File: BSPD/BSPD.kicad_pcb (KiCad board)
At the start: 2 copper layers, 66 x 42 mm, 66 parts, among them J2 282834-6, K2 G5Q-1A, Q1 BSS84, Q2 MMBT2222A, Q3 MMBT2222A, U1 LM339, U2 LM339, U3 74LVC2G00, U5 74LVC2G04, U6 LM311, U7 LM555xM, U8 74AHC1G32, U9 AMS1117-5.0

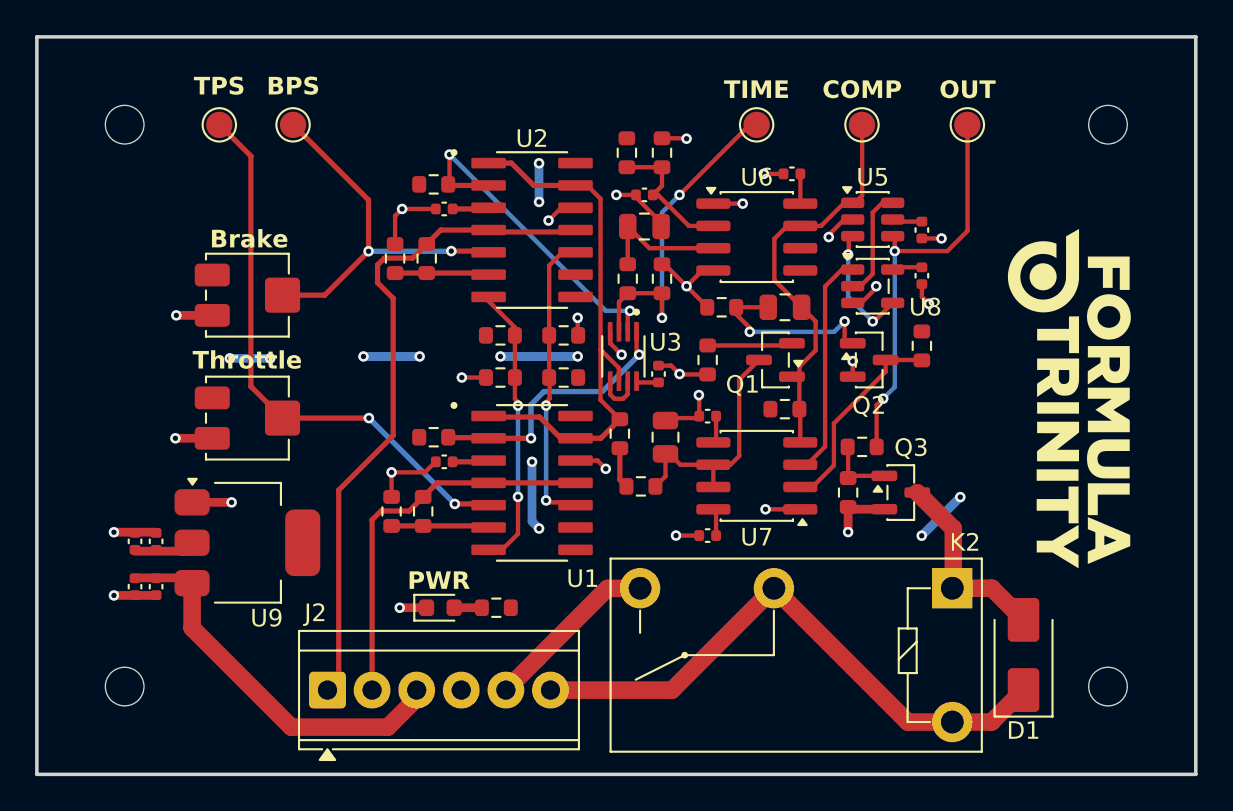
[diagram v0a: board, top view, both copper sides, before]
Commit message: v0.2
updated design, fixed trimmers, added extra debug LEDs.
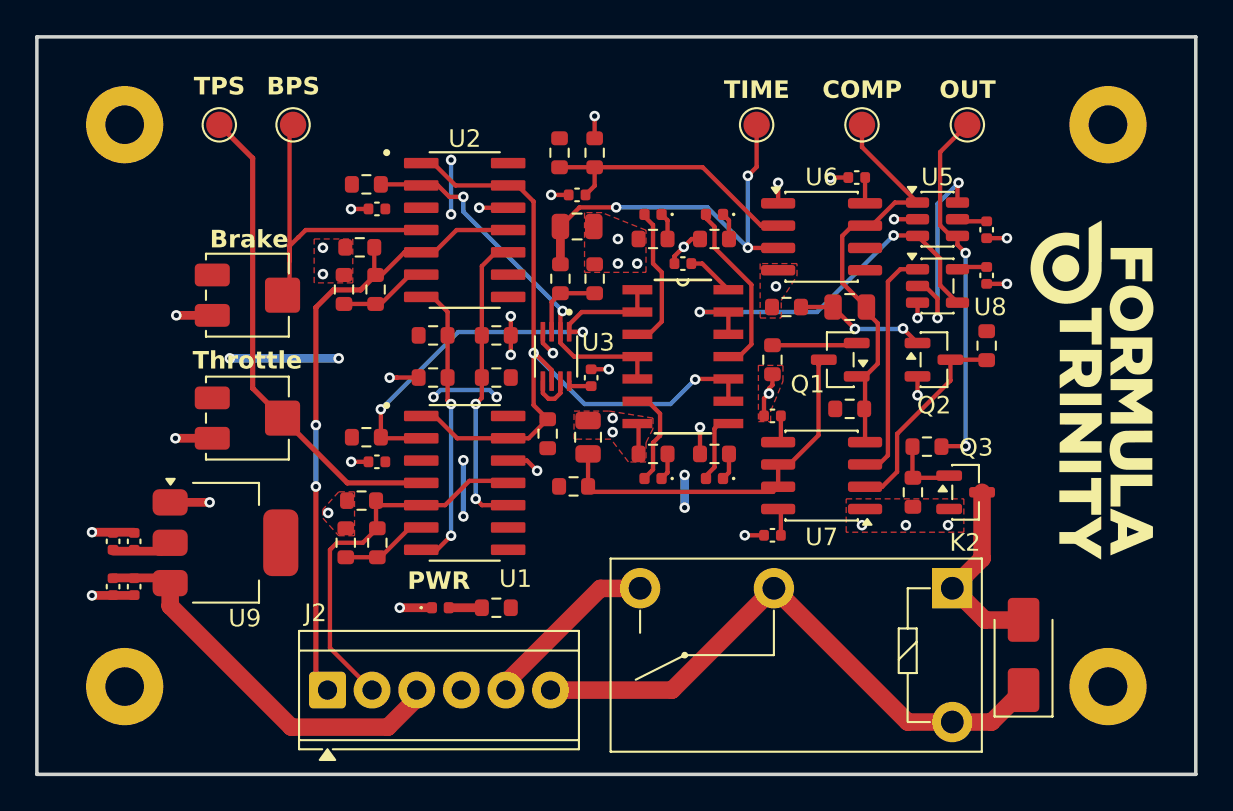
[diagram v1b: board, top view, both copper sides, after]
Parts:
- added C17: 100n, Capacitor_SMD:C_0402_1005Metric, F.Cu at (145.4, 95.7)
- added D3: SCS_Fault, LED_SMD:LED_0402_1005Metric, F.Cu at (147.2, 107.9)
- added D4: TPS_Fault, LED_SMD:LED_0402_1005Metric, F.Cu at (143.7, 92.9)
- added D5: BPS_Fault, LED_SMD:LED_0402_1005Metric, F.Cu at (143.7, 107.9)
- added D6: OUTPUT, LED_SMD:LED_0402_1005Metric, F.Cu at (147.2, 92.9)
- added R24: 4k7, Resistor_SMD:R_0603_1608Metric, F.Cu at (147.2, 106.5)
- added R25: 4k7, Resistor_SMD:R_0603_1608Metric, F.Cu at (143.7, 94.3)
- added R26: 4k7, Resistor_SMD:R_0603_1608Metric, F.Cu at (143.7, 106.5)
- added R27: 4k7, Resistor_SMD:R_0603_1608Metric, F.Cu at (147.2, 94.3)
- added R28: 100k, Resistor_SMD:R_0603_1608Metric, F.Cu at (127.1, 109.2)
- added R29: 100k, Resistor_SMD:R_0603_1608Metric, F.Cu at (127.0, 94.8)
- added U4: 74HC00, 74HC00D_653:SOIC127P600X175-14N, F.Cu at (145.4, 101.0)
- D2: footprint LED_SMD:LED_0603_1608Metric -> LED_SMD:LED_0402_1005Metric
- H1, H2, H3, H4: footprint MountingHole:MountingHole_2.2mm_M2 -> MountingHole:MountingHole_2.2mm_M2_Pad
- R18: value 100 -> 1k
- moved C11 4.41 mm to (140.0, 105.6)
- moved R7 4.11 mm to (137.7, 105.4)
- moved C9 3.84 mm to (140.2, 102.2)
- moved C3 3.84 mm to (128.0, 92.6)
- moved C4 3.84 mm to (128.0, 107.0)
- moved C5 3.84 mm to (139.4, 91.8)
- moved C6 3.84 mm to (139.4, 93.6)
- moved R12 3.84 mm to (140.4, 89.4)
- moved R13 3.84 mm to (140.4, 96.6)
- moved R14 3.84 mm to (138.4, 89.4)
- moved R5 3.84 mm to (127.4, 105.6)
- moved R6 3.84 mm to (127.4, 91.2)
- moved R8 3.84 mm to (134.8, 102.2)
- moved R9 3.84 mm to (134.8, 99.8)
- moved U1 3.84 mm to (133.0, 108.2)
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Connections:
- RV1 pad 2: Net-(U1A-+) -> Net-(U1A--)
- RV2 pad 2: Net-(U2A-+) -> Net-(U2A--)
- TP1 pad 1: Net-(U1A-+) -> Net-(U1A--)
- TP2 pad 1: Net-(U2A-+) -> Net-(U2A--)
- TP3 pad 1: Net-(R13-Pad1) -> Net-(U6--)
- U1 pad 4: Throttle Input -> Net-(U1A--)
- U1 pad 5: Net-(U1A-+) -> Throttle Input
- U2 pad 4: Brake Input -> Net-(U2A--)
- U2 pad 5: Net-(U2A-+) -> Brake Input
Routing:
- net Net-(U1A-+): track 32.0 -> 0.00 mm, vias 2 -> 0
- net Net-(U1A--): track 0.00 -> 27.6 mm
- net Net-(U2A-+): track 21.8 -> 0.00 mm, vias 2 -> 0
- net Net-(U2A--): track 0.00 -> 18.7 mm
- net GND: track 62.1 -> 43.6 mm, vias 28 -> 40
- net Net-(U6--): track 7.54 -> 23.2 mm, vias 0 -> 3
- net Net-(R13-Pad1): track 19.2 -> 4.35 mm, vias 2 -> 0
- net Net-(U4-Pad12): track 7.06 -> 21.9 mm
- net Net-(R7-Pad2): track 31.0 -> 44.4 mm, vias 0 -> 2
- net Net-(D6-A): track 0.00 -> 10.1 mm
- net Net-(R5-Pad2): track 15.4 -> 23.9 mm
- net Net-(D4-A): track 0.00 -> 8.22 mm
- net Net-(Q1-D): track 14.0 -> 21.6 mm
- net Net-(U6-+): track 7.97 -> 15.6 mm
- net Net-(D5-A): track 0.00 -> 5.64 mm
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- added copper zone on F.Cu, net GND
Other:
- board text added: "-BPS"
- board text added: "-GND"
- board text added: "-IN"
- board text added: "-OUT"
- board text added: "-TPS"
- board text added: "-VIN"
- board text added: "BALD MIHAO & JOHN CAVAN LTD."
- board text added: "IN & OUT - 12V"
- board text added: "TPS & BPS - 0.5-4.5V"
- board text added: "VIN - 12V"
- board text removed: "JOHN CAVAN INC."

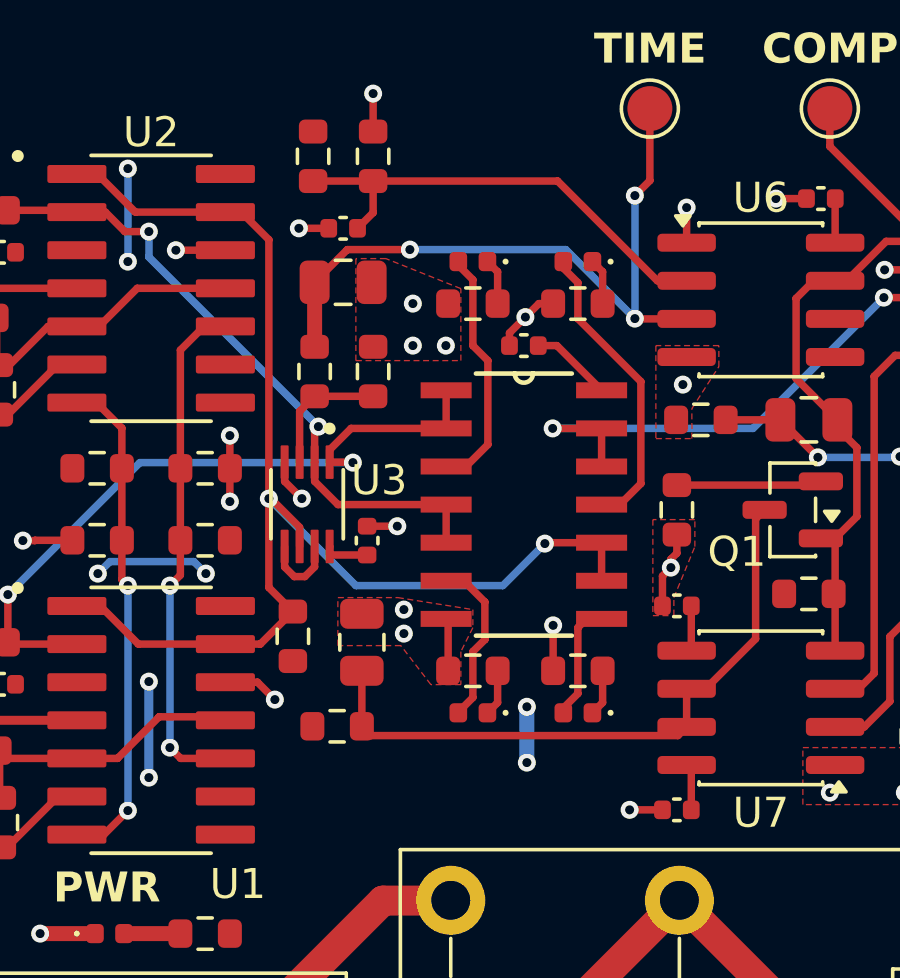
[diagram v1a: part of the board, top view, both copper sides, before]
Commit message: v0.3
minor silscreen changes
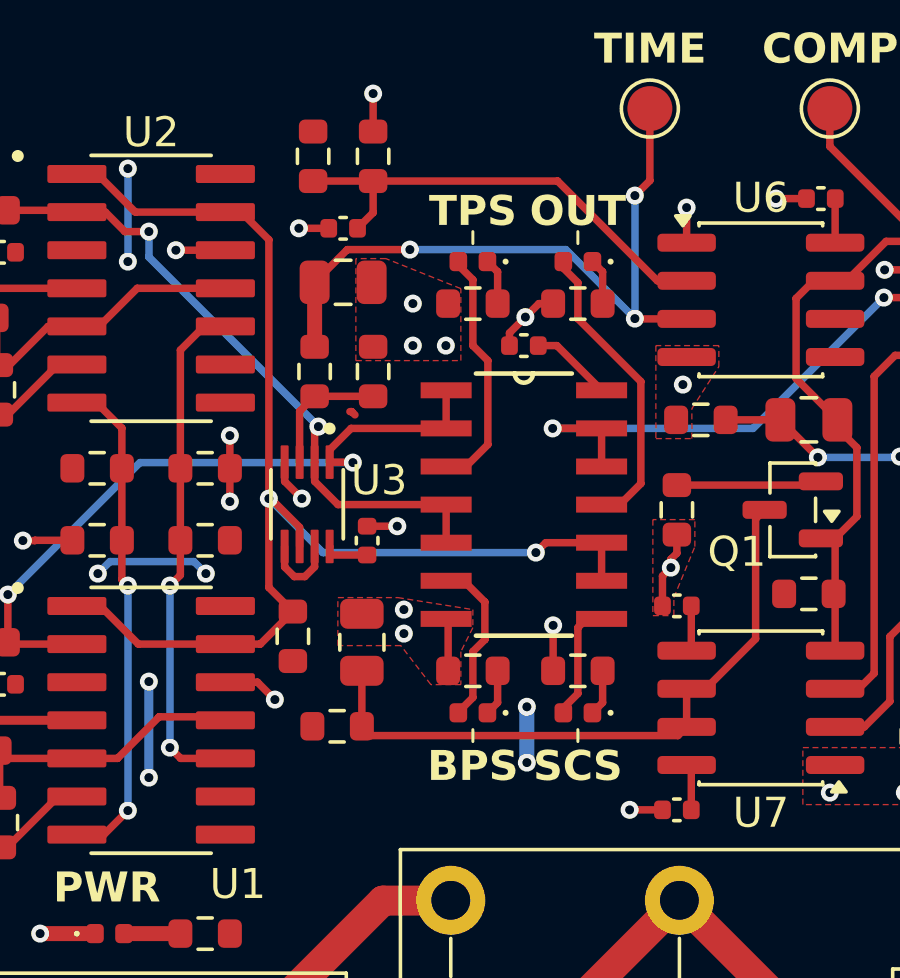
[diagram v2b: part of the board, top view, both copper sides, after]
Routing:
- net Net-(R7-Pad2): track 44.4 -> 43.5 mm
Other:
- board text added: "SCS"
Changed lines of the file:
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@@
 		)
+	)
+	(gr_line
+		(start 143.7 108.5)
+		(end 143.7 108.9)
+		(stroke
+			(width 0.1)
+			(type default)
+		)
+		(layer "F.SilkS")
+	)
+	(gr_line
+		(start 147.2 92.3)
+		(end 147.2 91.9)
+		(stroke
+			(width 0.1)
+			(type default)
+		)
+		(layer "F.SilkS")
+	)
+	(gr_line
+		(start 147.2 108.5)
+		(end 147.2 108.9)
+		(stroke
+			(width 0.1)
+			(type default)
+		)
+		(layer "F.SilkS")
+	)
+	(gr_line
+		(start 143.7 92.3)
+		(end 143.7 91.9)
+		(stroke
+			(width 0.1)
+			(type default)
+		)
+		(layer "F.SilkS")
 	)
 	(gr_rect
@@
 		)
 	)
+	(gr_text "TPS\n"
+		(at 143.7 91.8 0)
+		(layer "F.SilkS")
+		(effects
+			(font
+				(size 1 1)
+				(thickness 0.2)
+				(bold yes)
+			)
+			(justify bottom)
+		)
+	)
 	(gr_text "Brake"
 		(at 120.7 94.9 0)
@@
 		)
 	)
+	(gr_text "BPS"
+		(at 143.7 110.3 0)
+		(layer "F.SilkS")
+		(effects
+			(font
+				(size 1 1)
+				(thickness 0.2)
+				(bold yes)
+			)
+			(justify bottom)
+		)
+	)
 	(gr_text "PWR"
 		(at 131.5 114.35 0)
@@
 		)
 	)
+	(gr_text "OUT"
+		(at 147.2 91.8 0)
+		(layer "F.SilkS")
+		(effects
+			(font
+				(size 1 1)
+				(thickness 0.2)
+				(bold yes)
+			)
+			(justify bottom)
+		)
+	)
+	(gr_text "SCS"
+		(at 147.2 110.3 0)
+		(layer "F.SilkS")
+		(effects
+			(font
+				(size 1 1)
+				(thickness 0.2)
+				(bold yes)
+			)
+			(justify bottom)
+		)
+	)
 	(gr_text "BALD MIHAO & JOHN CAVAN LTD."
 		(at 141.6 85.6 0)
@@
 	)
 	(segment
+		(start 139.6 97.9)
+		(end 139.660582 97.9)
+		(width 0.25)
+		(layer "F.Cu")
+		(net 0)
+	)
+	(segment
+		(start 139.660582 97.9)
+		(end 139.769582 98.009)
+		(width 0.25)
+		(layer "F.Cu")
+		(net 0)
+	)
+	(segment
 		(start 112.95 113.6)
 		(end 115.82 113.6)
@@
 	)
 	(segment
-		(start 146.24 102.3)
-		(end 146.27 102.27)
-		(width 0.25)
-		(layer "F.Cu")
-		(net 28)
-	)
-	(segment
 		(start 136.9 100.8)
 		(end 136.9 103.765)
@@
 	)
 	(segment
+		(start 147.9908 102.27)
+		(end 146.13 102.27)
+		(width 0.25)
+		(layer "F.Cu")
+		(net 28)
+	)
+	(segment
 		(start 136.615 105.65)
 		(end 137.7 104.565)
@@
 	)
 	(segment
+		(start 146.13 102.27)
+		(end 145.8 102.6)
+		(width 0.25)
+		(layer "F.Cu")
+		(net 28)
+	)
+	(segment
 		(start 135.45 105.65)
 		(end 136.615 105.65)
@@
 	)
 	(segment
-		(start 146.1 102.3)
-		(end 146.24 102.3)
-		(width 0.25)
-		(layer "F.Cu")
-		(net 28)
-	)
-	(segment
 		(start 137.925 101.757802)
 		(end 137.925 102.395)
@@
 		(net 28)
 	)
-	(segment
-		(start 146.27 102.27)
-		(end 147.9908 102.27)
-		(width 0.25)
-		(layer "F.Cu")
+	(via
+		(at 145.8 102.6)
+		(size 0.6)
+		(drill 0.3)
+		(layers "F.Cu" "B.Cu")
 		(net 28)
 	)
 	(via
-		(at 146.1 102.3)
+		(at 136.9 100.8)
 		(size 0.6)
 		(drill 0.3)
@@
 		(net 28)
 	)
-	(via
-		(at 136.9 100.8)
-		(size 0.6)
-		(drill 0.3)
-		(layers "F.Cu" "B.Cu")
-		(net 28)
-	)
-	(segment
-		(start 139.8 103.7)
-		(end 144.7 103.7)
+	(segment
+		(start 138.7 102.6)
+		(end 136.9 100.8)
 		(width 0.25)
 		(layer "B.Cu")
@@
 	)
 	(segment
-		(start 144.7 103.7)
-		(end 146.1 102.3)
+		(start 145.8 102.6)
+		(end 138.7 102.6)
 		(width 0.25)
 		(layer "B.Cu")
-		(net 28)
-	)
-	(segment
-		(start 136.9 100.8)
-		(end 139.8 103.7)
-		(width 0.25)
-		(layer "B.Cu")

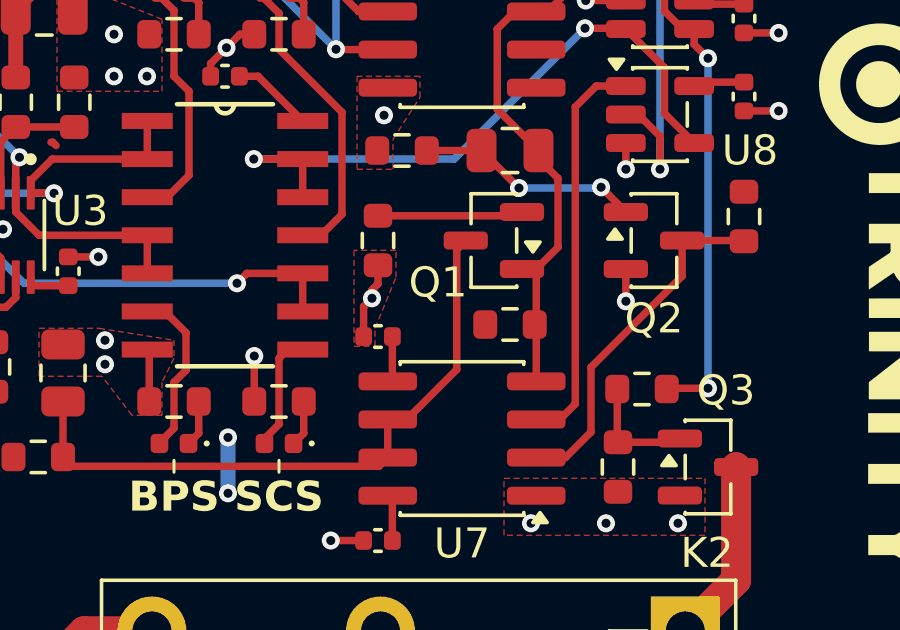
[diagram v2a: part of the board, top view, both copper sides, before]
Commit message: minor resistor changes and symbol correction
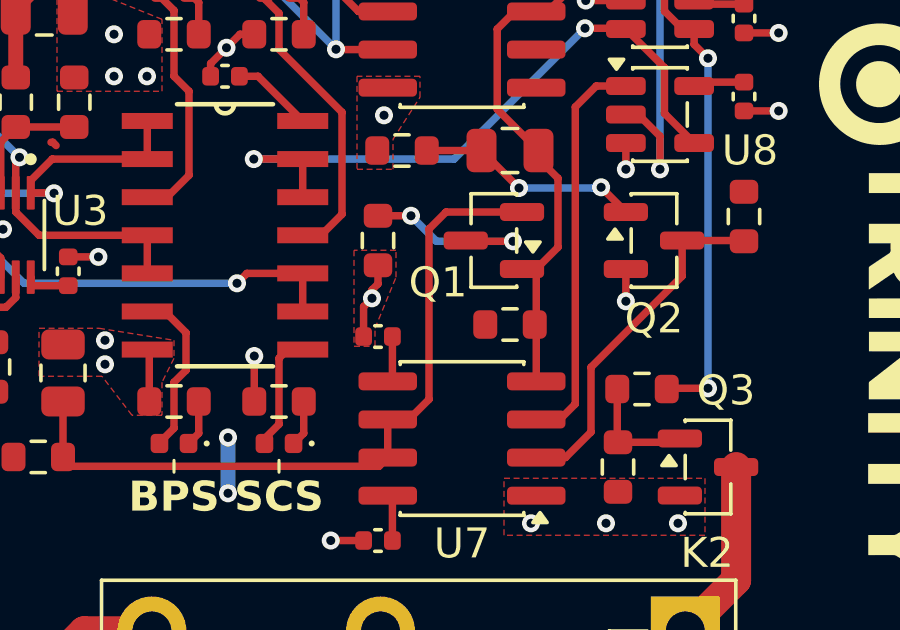
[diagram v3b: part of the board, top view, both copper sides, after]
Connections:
- C11 pad 1: Net-(Q1-D) -> Net-(Q1-S)
- R17 pad 2: Net-(Q1-S) -> Net-(Q1-D)
- R19 pad 2: Net-(Q1-D) -> Net-(Q1-S)
- U7 pad 6: Net-(Q1-D) -> Net-(Q1-S)
- U7 pad 7: Net-(Q1-D) -> Net-(Q1-S)
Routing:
- net Net-(Q1-S): track 4.85 -> 24.9 mm
- net Net-(Q1-D): track 21.6 -> 6.44 mm, vias 0 -> 2
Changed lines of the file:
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@@
 			(layers "F.Cu" "F.Mask" "F.Paste")
 			(roundrect_rratio 0.25)
-			(net 9 "Net-(Q1-S)")
+			(net 8 "Net-(Q1-D)")
 			(pintype "passive")
 		)
@@
 			(layers "F.Cu" "F.Mask" "F.Paste")
 			(roundrect_rratio 0.25)
-			(net 8 "Net-(Q1-D)")
+			(net 9 "Net-(Q1-S)")
 			(pintype "passive")
 		)
@@
 			(layers "F.Cu" "F.Mask" "F.Paste")
 			(roundrect_rratio 0.25)
-			(net 8 "Net-(Q1-D)")
+			(net 9 "Net-(Q1-S)")
 			(pintype "passive")
 		)
@@
 			(layers "F.Cu" "F.Mask" "F.Paste")
 			(roundrect_rratio 0.25)
-			(net 8 "Net-(Q1-D)")
+			(net 9 "Net-(Q1-S)")
 			(pinfunction "THRES")
 			(pintype "input")
@@
 			(layers "F.Cu" "F.Mask" "F.Paste")
 			(roundrect_rratio 0.25)
-			(net 8 "Net-(Q1-D)")
+			(net 9 "Net-(Q1-S)")
 			(pinfunction "DISCH")
 			(pintype "input")
@@
 	)
 	(segment
-		(start 150.825 107.14)
-		(end 150.825 108.41)
+		(start 151.6 100.35)
+		(end 150.5 100.35)
 		(width 0.25)
 		(layer "F.Cu")
@@
 	)
 	(segment
-		(start 140.31 108.7)
-		(end 150.535 108.7)
+		(start 153.45 101.2)
+		(end 153.425 101.175)
 		(width 0.25)
 		(layer "F.Cu")
@@
 	)
 	(segment
-		(start 153.125 105.475)
-		(end 151.46 107.14)
+		(start 155 101.2)
+		(end 153.45 101.2)
 		(width 0.25)
 		(layer "F.Cu")
 		(net 8)
 	)
+	(via
+		(at 155 101.2)
+		(size 0.6)
+		(drill 0.3)
+		(layers "F.Cu" "B.Cu")
+		(net 8)
+	)
+	(via
+		(at 151.6 100.35)
+		(size 0.6)
+		(drill 0.3)
+		(layers "F.Cu" "B.Cu")
+		(net 8)
+	)
 	(segment
-		(start 153.125 101.475)
-		(end 153.125 105.475)
+		(start 151.6 100.35)
+		(end 152.45 101.2)
 		(width 0.25)
-		(layer "F.Cu")
+		(layer "B.Cu")
 		(net 8)
 	)
 	(segment
-		(start 150.805 108.39)
+		(start 152.45 101.2)
+		(end 155 101.2)
+		(width 0.25)
+		(layer "B.Cu")
+		(net 8)
+	)
+	(segment
+		(start 152.2 100.792589)
+		(end 152.2 106.47)
+		(width 0.25)
+		(layer "F.Cu")
+		(net 9)
+	)
+	(segment
+		(start 150.825 107.14)
 		(end 150.825 108.41)
 		(width 0.25)
 		(layer "F.Cu")
-		(net 8)
+		(net 9)
 	)
 	(segment
-		(start 151.46 107.14)
+		(start 140.31 108.7)
+		(end 150.535 108.7)
+		(width 0.25)
+		(layer "F.Cu")
+		(net 9)
+	)
+	(segment
+		(start 152.767589 100.225)
+		(end 152.2 100.792589)
+		(width 0.25)
+		(layer "F.Cu")
+		(net 9)
+	)
+	(segment
+		(start 151.53 107.14)
 		(end 150.825 107.14)
 		(width 0.25)
 		(layer "F.Cu")
-		(net 8)
+		(net 9)
 	)
 	(segment
-		(start 150.535 108.7)
+		(start 150.805 108.39)
 		(end 150.825 108.41)
 		(width 0.25)
 		(layer "F.Cu")
-		(net 8)
+		(net 9)
 	)
 	(segment
-		(start 140 108.39)
-		(end 140.31 108.7)
+		(start 152.2 106.47)
+		(end 151.53 107.14)
 		(width 0.25)
 		(layer "F.Cu")
-		(net 8)
+		(net 9)
 	)
 	(segment
-		(start 140 106.54)
-		(end 140 108.39)
+		(start 150.535 108.7)
+		(end 150.825 108.41)
 		(width 0.25)
 		(layer "F.Cu")
-		(net 8)
+		(net 9)
 	)
 	(segment
-		(start 153.425 101.175)
-		(end 153.125 101.475)
+		(start 140 108.39)
+		(end 140.31 108.7)
 		(width 0.25)
 		(layer "F.Cu")
-		(net 8)
+		(net 9)
 	)
 	(segment
-		(start 150.5 100.35)
-		(end 155.175 100.35)
+		(start 155.3 100.225)
+		(end 152.767589 100.225)
 		(width 0.25)
 		(layer "F.Cu")
@@
 	)
 	(segment
-		(start 155.175 100.35)
-		(end 155.3 100.225)
+		(start 140 106.54)
+		(end 140 108.39)
 		(width 0.25)
 		(layer "F.Cu")

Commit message: minor changes
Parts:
- D2, D3, D4, D5, D6: footprint LED_SMD:LED_0402_1005Metric -> LED_SMD:LED_0603_1608Metric
- R23: value 1k -> 330
- R24, R25, R26, R27: value 4k7 -> 330
- R28, R29: value 100k -> 470k
- moved D4 0.30 mm to (143.7, 92.6)
- moved D6 0.30 mm to (147.2, 92.6)
- moved D3 0.26 mm to (147.2, 108.2)
- moved D5 0.26 mm to (143.7, 108.2)
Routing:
- net +5V: track 32.5 -> 33.6 mm
- net Net-(Q1-S): track 24.9 -> 25.4 mm

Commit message: v0.4
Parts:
- added R30: 10k, Resistor_SMD:R_0603_1608Metric, F.Cu at (128.4, 95.9)
- R18: value 1k -> 2.2k
- R23, R24, R25, R26, R27: value 330 -> 220
- R28, R29: value 470k -> 100k
- moved R20 30.1 mm to (128.4, 110.3)
- moved R29 4.55 mm to (128.4, 99.1), turned to 90 degrees
- moved R28 4.47 mm to (128.4, 113.5), turned to 90 degrees
- moved R3 1.82 mm to (126.7, 110.3)
- moved R1 1.75 mm to (125.0, 110.3)
- moved R4 1.75 mm to (126.7, 95.9)
- moved R2 1.68 mm to (125.0, 95.9)
- moved Q3 1.50 mm to (160.0, 108.7)
- moved R18 0.60 mm to (159.9, 106.1)
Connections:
- R20 pad 1: Net-(Q3-B) -> TPS
- R20 pad 2: GND -> Throttle Input
- R3 pad 2: Throttle Input -> TPS
- R4 pad 2: Brake Input -> BPS
- U1 pad 11: Throttle Input -> TPS
- U1 pad 5: Throttle Input -> TPS
- U2 pad 11: Brake Input -> BPS
- U2 pad 5: Brake Input -> BPS
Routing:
- net Throttle Input: track 22.1 -> 9.38 mm
- net Brake Input: track 37.4 -> 26.5 mm
- net TPS: track 0.00 -> 9.29 mm
- net BPS: track 0.00 -> 9.28 mm
- net +5V: track 33.6 -> 42.7 mm, vias 10 -> 13
- net GND: track 43.6 -> 50.2 mm, vias 40 -> 39
- net Net-(U6--): track 23.3 -> 26.2 mm, vias 3 -> 0
- net Net-(Q3-B): track 3.90 -> 1.66 mm
- net Net-(U1B--): track 6.11 -> 7.20 mm
- net Net-(R18-Pad1): track 21.2 -> 20.1 mm
- net Net-(U2B--): track 5.09 -> 5.95 mm
- net Net-(D1-A): track 11.0 -> 10.4 mm
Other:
- board text added: "IN & OUT ~ 12V"
- board text added: "TPS & BPS ~ 0.5-4.5V"
- board text added: "VIN ~ 12V"
- board text removed: "IN & OUT - 12V"
- board text removed: "TPS & BPS - 0.5-4.5V"
- board text removed: "VIN - 12V"
